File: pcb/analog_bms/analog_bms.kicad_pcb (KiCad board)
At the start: 2 copper layers, 42 x 22 mm, 55 parts, among them J1 Screw_Terminal_1x2, J2 MODULE+, J3 MODULE-, Q1 PMOS, Q2 NMOS, Q3 PMOS, Q4 NMOS, Q5 PMOS, U1 TLV7031DBV, U2 TLV7031DBV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

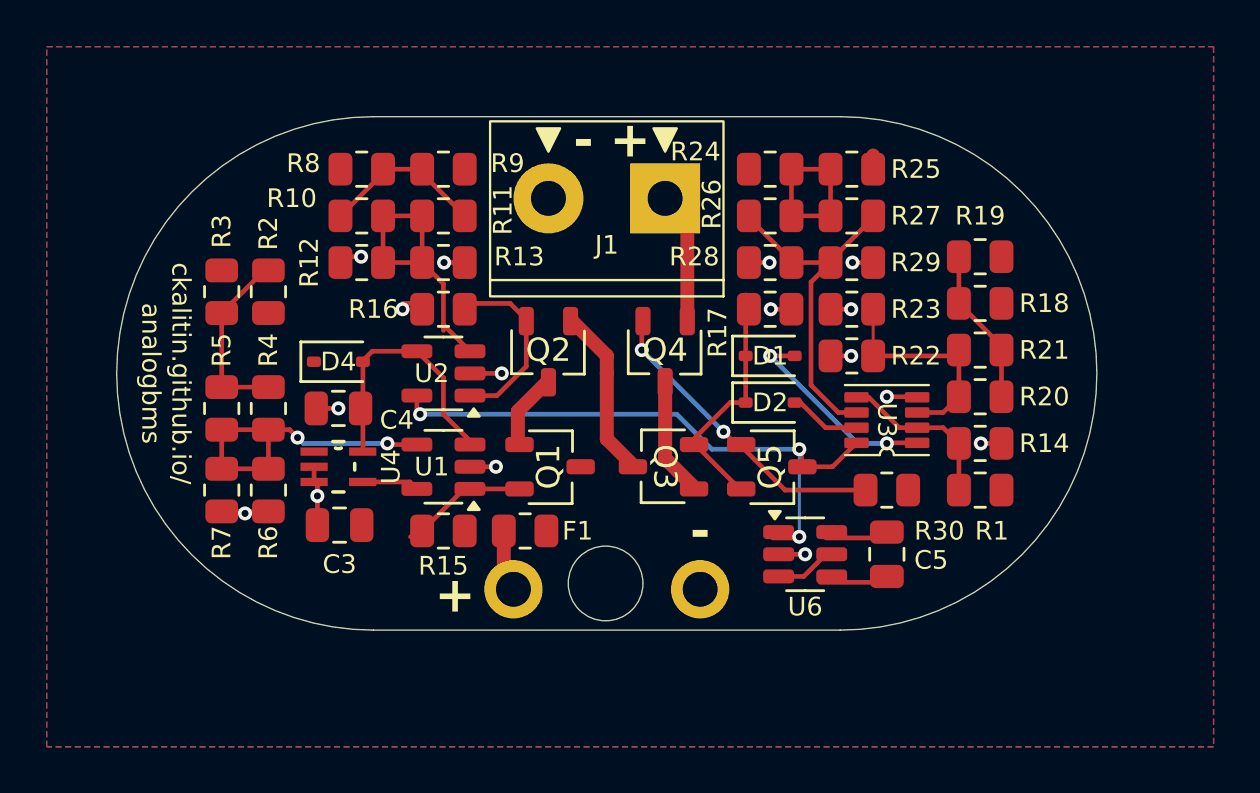
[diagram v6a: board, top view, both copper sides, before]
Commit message: Fix comparator + pour to track dist
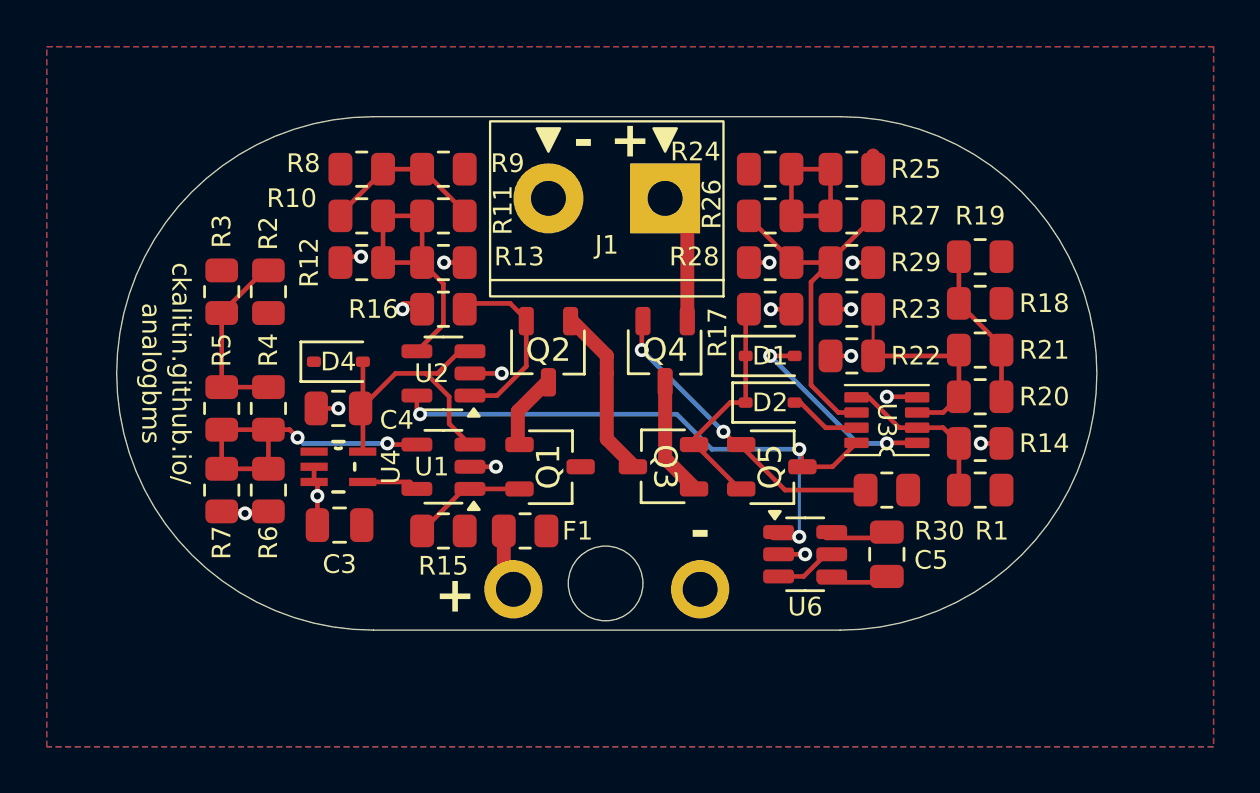
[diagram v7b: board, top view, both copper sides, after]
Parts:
- removed the G*** at (150.2, 119.5)
- added G***: LOGO, LOGO, B.Cu at (123.0, 119.0)
- added G***: LOGO, LOGO, B.Cu at (129.8, 116.5)
- added G***: LOGO, LOGO, B.Cu at (129.8, 122.0)
- added G***: LOGO, LOGO, B.Cu at (147.8, 107.0)
- R1: value Thermistor_NTC -> Thermistor_PTC
- moved G*** 3.81 mm to (123.8, 112.8)
- moved G*** 2.55 mm to (130.0, 107.0)
- moved G*** 0.09 mm to (154.2, 111.2)
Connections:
- R10 pad 2: Net-(U2-+) -> Net-(U2--)
- R11 pad 2: Net-(U2-+) -> Net-(U2--)
- R12 pad 1: Net-(U2-+) -> Net-(U2--)
- R13 pad 1: Net-(U2-+) -> Net-(U2--)
- U2 pad 3: Net-(U2-+) -> Net-(D4-A)
- U2 pad 4: Net-(D4-A) -> Net-(U2--)
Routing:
- net Net-(U2-+): track 12.2 -> 0.00 mm
- net Net-(U2--): track 0.00 -> 12.0 mm
- net Net-(D4-A): track 11.3 -> 13.4 mm
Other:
- copper layers 2 -> 4
- rule solder_mask_min_width: 0.1016 -> 0.12
- board text added: "stop giving a fuck about what random normies think of u thats like playing oblivion and not jumping everywherebecause u dont want the npcs to think ur weird"

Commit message: Digikey, TI, and PCBWay orders!
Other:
- copper layers 4 -> 2
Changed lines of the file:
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@@
 	(layers
 		(0 "F.Cu" signal "Front")
-		(4 "In1.Cu" signal)
-		(6 "In2.Cu" signal)
 		(2 "B.Cu" signal "Back")
 		(13 "F.Paste" user)
@@
 				(type "core")
 				(color "#808080FF")
-				(thickness 0.480066)
-				(material "FR4")
-				(epsilon_r 4.5)
-				(loss_tangent 0.02)
-			)
-			(layer "In1.Cu"
-				(type "copper")
-				(thickness 0.035)
-			)
-			(layer "dielectric 2"
-				(type "prepreg")
-				(thickness 0.480066)
-				(material "FR4")
-				(epsilon_r 4.5)
-				(loss_tangent 0.02)
-			)
-			(layer "In2.Cu"
-				(type "copper")
-				(thickness 0.035)
-			)
-			(layer "dielectric 3"
-				(type "core")
-				(thickness 0.480066)
+				(thickness 1.510198)
 				(material "FR4")
 				(epsilon_r 4.5)
@@
 		)
 		(pad_to_mask_clearance 0)
-		(solder_mask_min_width 0.12)
 		(allow_soldermask_bridges_in_footprints no)
 		(tenting front back)
@@
 			(disableapertmacros no)
 			(usegerberextensions no)
-			(usegerberattributes yes)
-			(usegerberadvancedattributes yes)
-			(creategerberjobfile yes)
+			(usegerberattributes no)
+			(usegerberadvancedattributes no)
+			(creategerberjobfile no)
 			(dashed_line_dash_ratio 12.000000)
 			(dashed_line_gap_ratio 3.000000)
@@
 			(outputformat 1)
 			(mirror no)
-			(drillshape 1)
+			(drillshape 0)
 			(scaleselection 1)
-			(outputdirectory "")
+			(outputdirectory "gerbers/")
 		)
 	)
